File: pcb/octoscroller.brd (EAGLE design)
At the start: 71.8 x 54.6 mm, 5 parts

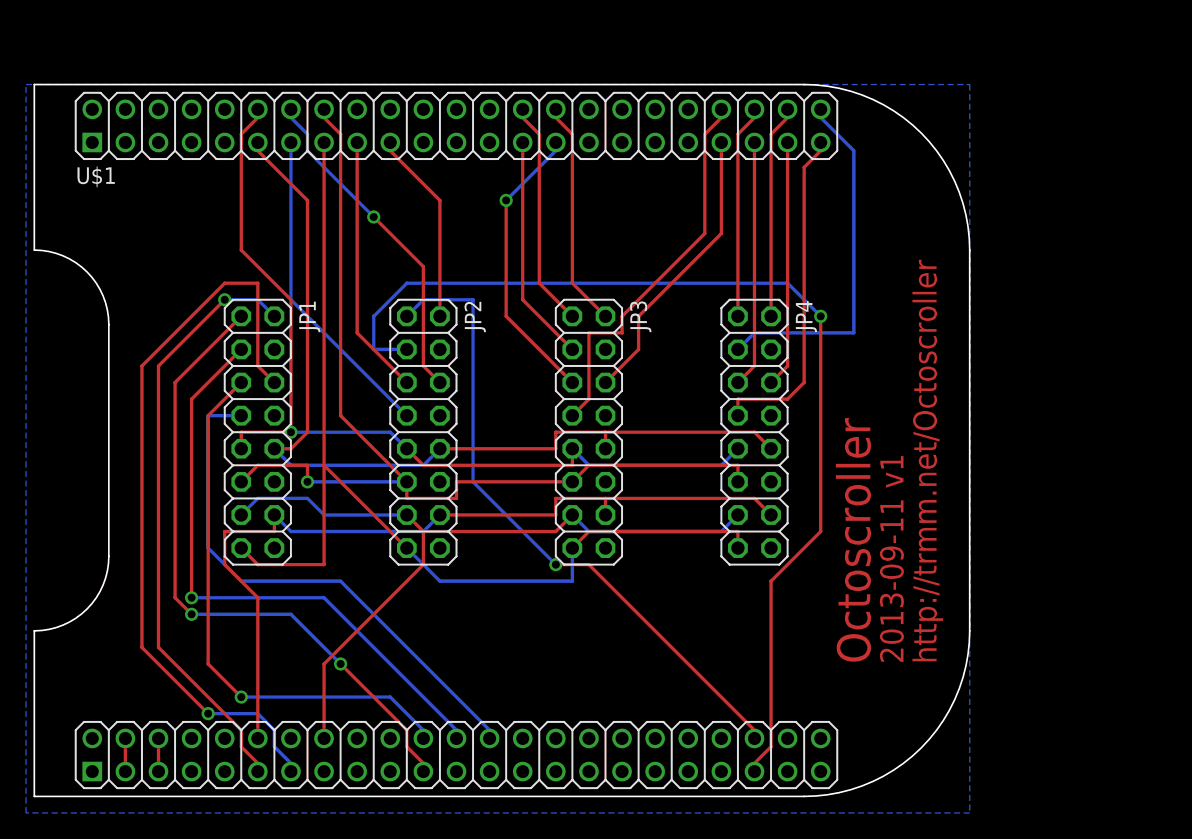
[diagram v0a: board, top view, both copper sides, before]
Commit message: octoscroller gets octo-outputs
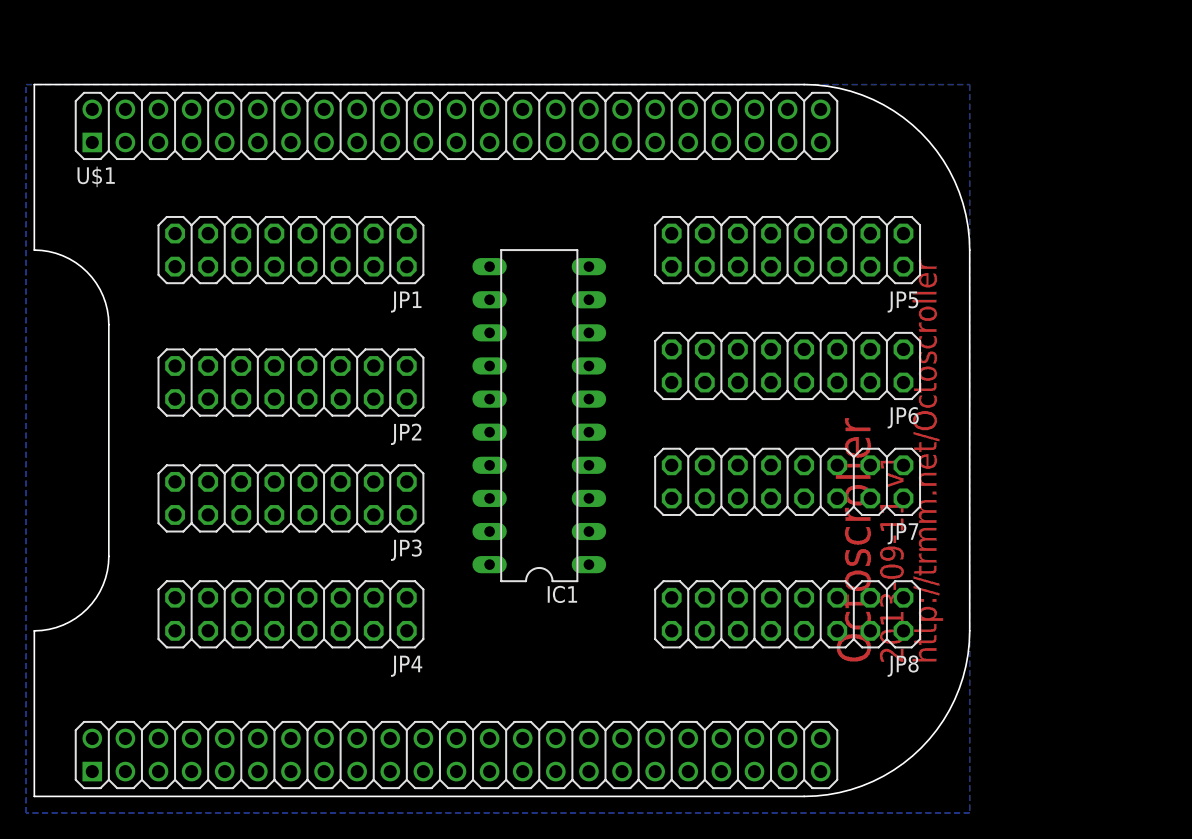
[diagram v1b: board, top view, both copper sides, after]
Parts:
- added IC1: 74LS245N, adafruit:DIL20
- added JP5, JP6, JP7, JP8: (no value), pinhead:2X08
- moved JP4 38.2 mm to (36.8, 29.2), turned to 180 degrees
- moved JP3 23.4 mm to (36.8, 38.1), turned to 180 degrees
- moved JP1 14.2 mm to (36.8, 57.1), turned to 180 degrees
- moved JP2 10.9 mm to (36.8, 47.0), turned to 180 degrees
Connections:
- new net D: JP1.12, JP2.12, JP3.12, JP4.12, JP5.12, JP6.12, JP7.12, JP8.12, U$1.15
- new net N$1: IC1.18
- new net VCC: IC1.20
- net A: now also JP5.9, JP6.9, JP7.9, JP8.9
- net B: now also JP5.10, JP6.10, JP7.10, JP8.10
- net B1: now also JP2.3, JP3.3, JP4.3, JP5.3, JP6.3, JP7.3, JP8.3
- net B2: now also JP2.7, JP3.7, JP4.7, JP5.7, JP6.7, JP7.7, JP8.7
- net B3: no longer JP2.3
- net B4: no longer JP2.7
- net B5: no longer JP3.3
- net B6: no longer JP3.7
- net B7: no longer JP4.3
- net B8: no longer JP4.7
- net C: now also JP5.11, JP6.11, JP7.11, JP8.11
- net CLK: now also JP5.13, JP6.13, JP7.13, JP8.13
- net G1: now also JP2.2, JP3.2, JP4.2, JP5.2, JP6.2, JP7.2, JP8.2
- net G2: now also JP2.6, JP3.6, JP4.6, JP5.6, JP6.6, JP7.6, JP8.6
- net G3: no longer JP2.2
- net G4: no longer JP2.6
- net G5: no longer JP3.2
- net G6: no longer JP3.6
- net G7: no longer JP4.2
- net G8: no longer JP4.6
- net GND: now also IC1.10, JP5.16, JP5.4, JP5.8, JP6.16, JP6.4, JP6.8, JP7.16, JP7.4, JP7.8, JP8.16, JP8.4, JP8.8; no longer JP1.12, JP2.12, JP3.12, JP4.12
- net LATCH: now also JP5.14, JP6.14, JP7.14, JP8.14
- net OE: now also JP5.15, JP6.15, JP7.15, JP8.15, U$1.26; no longer U$1.15
- net R1: now also JP2.1, JP3.1, JP4.1, JP5.1, JP6.1, JP7.1, JP8.1
- net R2: now also JP2.5, JP3.5, JP4.5, JP5.5, JP6.5, JP7.5, JP8.5
- net R3: no longer JP2.1
- net R4: no longer JP2.5
- net R5: no longer JP3.1
- net R6: no longer JP3.5
- net R7: no longer JP4.1
- net R8: no longer JP4.5
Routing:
- net OE: track 79.0 -> 0.00 mm
- net B3: track 78.5 -> 0.00 mm, vias 1 -> 0
- net C: track 75.4 -> 0.00 mm, vias 1 -> 0
- net A: track 69.6 -> 0.00 mm, vias 1 -> 0
- net B: track 69.1 -> 0.00 mm
- net LATCH: track 64.2 -> 0.00 mm
- net CLK: track 60.3 -> 0.00 mm
- net G2: track 57.7 -> 0.00 mm, vias 1 -> 0
- net R3: track 49.7 -> 0.00 mm, vias 1 -> 0
- net R1: track 49.4 -> 0.00 mm, vias 2 -> 0
- net G1: track 45.8 -> 0.00 mm, vias 1 -> 0
- net B1: track 45.8 -> 0.00 mm, vias 1 -> 0
- net R2: track 41.9 -> 0.00 mm, vias 1 -> 0
- net B2: track 40.7 -> 0.00 mm
- net B6: track 29.7 -> 0.00 mm
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
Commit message: octoscroller renamed outputs
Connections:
- removed net B4: U$1.13
- removed net B5: U$1.27
- removed net G3: U$1.19
- removed net G4: U$1.14
- removed net G5: U$1.30
- removed net N$1: IC1.18
- removed net R4: U$1.17
- removed net R5: U$1.28
- removed net R6: U$1.29
- new net A_RAW: IC1.18, U$1.12
- new net B1.1: JP1.3, U$1.9
- new net B1.2: JP1.7, U$1.14
- new net B2.1: JP2.3, U$1.19
- new net B2.2: JP2.7, U$1.28
- new net B3.1: JP3.3
- new net B3.2: JP3.7
- new net B4.1: JP4.3
- new net B4.2: JP4.7
- new net B5.1: JP5.3
- new net B5.2: JP5.7
- new net B6.1: JP6.3
- new net B6.2: JP6.7
- new net B7.1: JP7.3
- new net B7.2: JP7.7
- new net B8.1: JP8.3
- new net B8.2: JP8.7
- new net B_RAW: IC1.17, U$1.11
- new net CLK_RAW: IC1.13, U$1.62
- new net C_RAW: IC1.16, U$1.16
- new net D_RAW: IC1.15, U$1.15
- new net G1.1: JP1.2, U$1.8
- new net G1.2: JP1.6, U$1.10
- new net G2.1: JP2.2, U$1.18
- new net G2.2: JP2.6, U$1.29
- new net G3.1: JP3.2
- new net G3.2: JP3.6
- new net G4.1: JP4.2
- new net G4.2: JP4.6
- new net G5.1: JP5.2
- new net G5.2: JP5.6
- new net G6.1: JP6.2
- new net G6.2: JP6.6
- new net G7.1: JP7.2
- new net G7.2: JP7.6
- new net G8.1: JP8.2
- new net G8.2: JP8.6
- new net LATCH_RAW: IC1.12, U$1.58
- new net N$11: U$1.32
- new net N$12: U$1.34
- new net N$13: U$1.36
- new net N$14: U$1.38
- new net N$15: U$1.61
- new net N$16: U$1.63
- new net N$17: U$1.69
- new net N$18: U$1.71
- new net N$19: U$1.73
- new net N$20: U$1.75
- new net N$21: U$1.77
- new net N$22: U$1.60
- new net N$23: U$1.74
- new net N$24: U$1.76
- new net N$4: U$1.31
- new net N$5: U$1.33
- new net N$6: U$1.35
- new net N$7: U$1.37
- new net OE_RAW: IC1.14, U$1.26
- new net R1.1: JP1.1, U$1.7
- new net R1.2: JP1.5, U$1.13
- new net R2.1: JP2.1, U$1.17
- new net R2.2: JP2.5, U$1.27
- new net R3.1: JP3.1
- new net R3.2: JP3.5
- new net R4.1: JP4.1
- new net R4.2: JP4.5
- new net R5.1: JP5.1, U$1.30
- new net R5.2: JP5.5
- new net R6.1: JP6.1
- new net R6.2: JP6.5
- new net R7.1: JP7.1
- new net R7.2: JP7.5
- new net R8.1: JP8.1
- new net R8.2: JP8.5
- net A: now also IC1.2; no longer U$1.12
- net B: now also IC1.3; no longer U$1.11
- net B1: no longer JP1.3, JP2.3, JP3.3, JP4.3, JP5.3, JP6.3, JP7.3, JP8.3
- net B2: no longer JP1.7, JP2.7, JP3.7, JP4.7, JP5.7, JP6.7, JP7.7, JP8.7
- net C: now also IC1.4; no longer U$1.16
- net CLK: now also IC1.7; no longer U$1.62
- net D: now also IC1.5; no longer U$1.15
- net G1: no longer JP1.2, JP2.2, JP3.2, JP4.2, JP5.2, JP6.2, JP7.2, JP8.2
- net G2: no longer JP1.6, JP2.6, JP3.6, JP4.6, JP5.6, JP6.6, JP7.6, JP8.6
- net GND: now also IC1.1, IC1.19
- net LATCH: now also IC1.8; no longer U$1.58
- net OE: now also IC1.6; no longer U$1.26
- net R1: no longer JP1.1, JP2.1, JP3.1, JP4.1, JP5.1, JP6.1, JP7.1, JP8.1
- net R2: no longer JP1.5, JP2.5, JP3.5, JP4.5, JP5.5, JP6.5, JP7.5, JP8.5

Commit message: As ordered from OSH Park
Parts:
- moved IC1 25.4 mm to (30.5, 43.2), flipped to the bottom, turned to 270 degrees
- moved JP4 13.0 mm to (49.5, 26.7), turned to 0 degrees
- moved JP1 12.8 mm to (49.5, 58.4), turned to 0 degrees
- moved JP2 12.8 mm to (49.5, 48.3), turned to 0 degrees
- moved JP3 12.8 mm to (49.5, 36.8), turned to 0 degrees
- moved JP7 2.84 mm to (76.2, 36.8), turned to 0 degrees
- moved JP8 2.84 mm to (76.2, 26.7), turned to 0 degrees
- moved JP5 1.80 mm to (76.2, 58.4), turned to 0 degrees
- moved JP6 1.27 mm to (76.2, 48.3), turned to 0 degrees
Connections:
- removed net B1: U$1.70
- removed net B2: U$1.72
- removed net B3: U$1.87
- removed net B6: U$1.40
- removed net B7: U$1.46
- removed net B8: U$1.45
- removed net G1: U$1.57
- removed net G2: U$1.59
- removed net G6: U$1.39
- removed net G7: U$1.44
- removed net G8: U$1.43
- removed net N$11: U$1.32
- removed net N$12: U$1.34
- removed net N$13: U$1.36
- removed net N$14: U$1.38
- removed net N$15: U$1.61
- removed net N$16: U$1.63
- removed net N$17: U$1.69
- removed net N$18: U$1.71
- removed net N$19: U$1.73
- removed net N$20: U$1.75
- removed net N$21: U$1.77
- removed net N$22: U$1.60
- removed net N$23: U$1.74
- removed net N$24: U$1.76
- removed net N$4: U$1.31
- removed net N$5: U$1.33
- removed net N$6: U$1.35
- removed net N$7: U$1.37
- removed net R1: U$1.67
- removed net R2: U$1.68
- removed net R3: U$1.88
- removed net R7: U$1.42
- removed net R8: U$1.41
- removed net SYS_5V: U$1.53
- removed net VCC: IC1.20
- new net +5V: IC1.20, U$1.53
- net B3.1: now also U$1.59
- net B3.2: now also U$1.63
- net B4.1: now also U$1.69
- net B4.2: now also U$1.64
- net B5.1: now also U$1.31
- net B5.2: now also U$1.34
- net B6.1: now also U$1.37
- net B6.2: now also U$1.39
- net B7.1: now also U$1.43
- net B7.2: now also U$1.46
- net B8.1: now also U$1.75
- net B8.2: now also U$1.87
- net G3.1: now also U$1.60
- net G3.2: now also U$1.67
- net G4.1: now also U$1.70
- net G4.2: now also U$1.73
- net G5.1: now also U$1.32
- net G5.2: now also U$1.35
- net G6.1: now also U$1.38
- net G6.2: now also U$1.41
- net G7.1: now also U$1.44
- net G7.2: now also U$1.88
- net G8.1: now also U$1.76
- net G8.2: now also U$1.72
- net R3.1: now also U$1.57
- net R3.2: now also U$1.61
- net R4.1: now also U$1.68
- net R4.2: now also U$1.71
- net R5.2: now also U$1.33
- net R6.1: now also U$1.36
- net R6.2: now also U$1.40
- net R7.1: now also U$1.42
- net R7.2: now also U$1.45
- net R8.1: now also U$1.74
- net R8.2: now also U$1.77
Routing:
- net D: track 0.00 -> 135.9 mm, vias 0 -> 1
- net LATCH: track 0.00 -> 129.2 mm, vias 0 -> 1
- net OE: track 0.00 -> 128.2 mm, vias 0 -> 1
- net CLK: track 0.00 -> 122.3 mm, vias 0 -> 1
- net C: track 0.00 -> 121.4 mm, vias 0 -> 1
- net B: track 0.00 -> 120.7 mm, vias 0 -> 2
- net A: track 0.00 -> 114.3 mm, vias 0 -> 2
- net B7.1: track 0.00 -> 57.2 mm, vias 0 -> 1
- net OE_RAW: track 0.00 -> 45.0 mm, vias 0 -> 2
- net B7.2: track 0.00 -> 43.6 mm
- net G7.1: track 0.00 -> 43.6 mm, vias 0 -> 1
- net R7.2: track 0.00 -> 42.8 mm, vias 0 -> 1
- net +5V: track 0.00 -> 39.9 mm
- net R7.1: track 0.00 -> 37.9 mm
- net G3.2: track 0.00 -> 35.9 mm, vias 0 -> 2
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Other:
- board text added: "2013-09-30"
- board text added: "Octoscroller^2"
- board text removed: "2013-09-11 v1"
- board text removed: "Octoscroller"

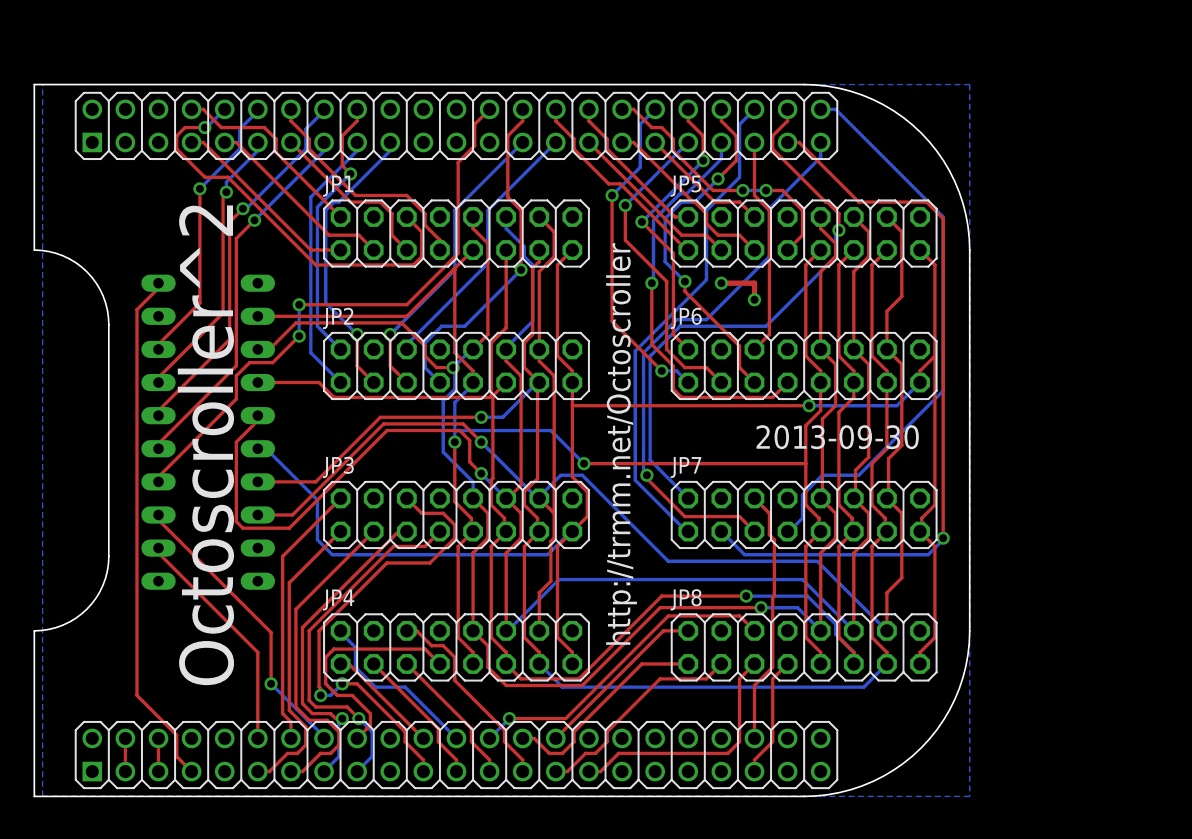
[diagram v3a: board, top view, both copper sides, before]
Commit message: reworked slightly to adjust position of connectors; ordered via oshpark
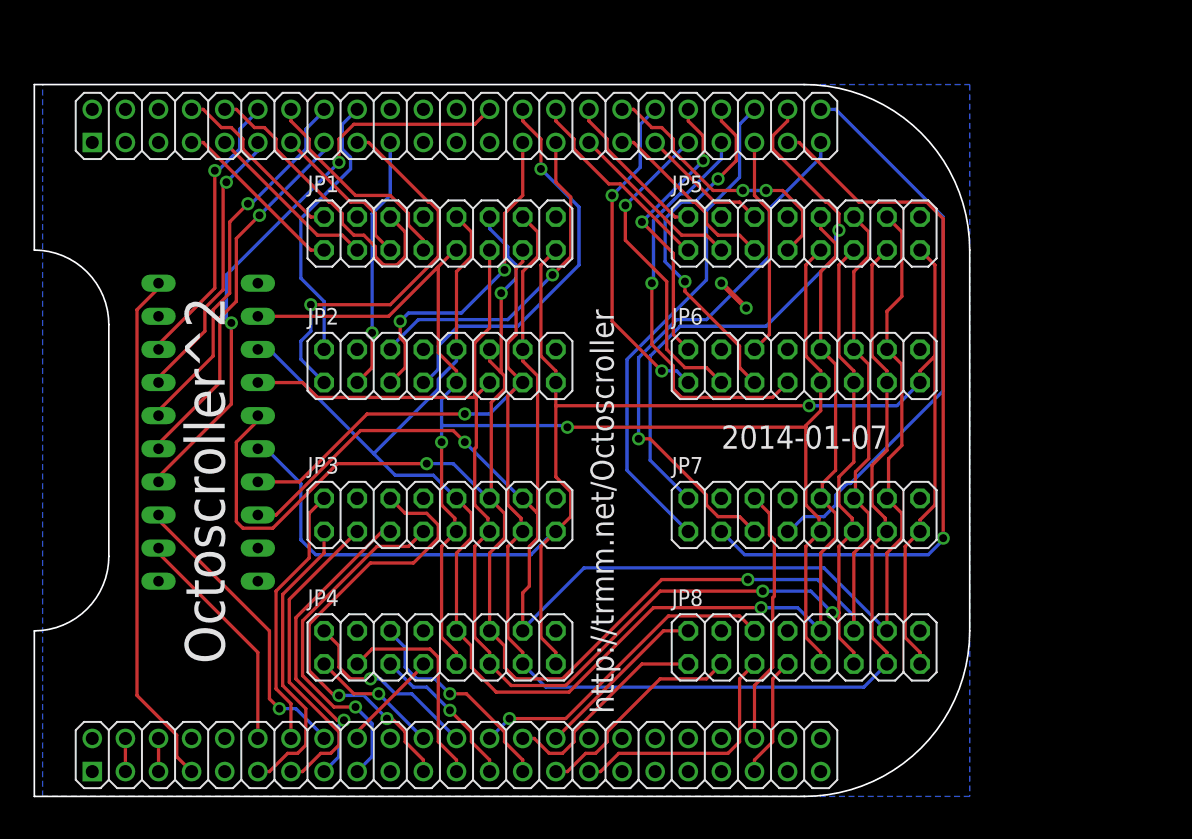
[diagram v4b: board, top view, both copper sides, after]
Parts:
- moved JP1 1.27 mm to (48.3, 58.4)
- moved JP2 1.27 mm to (48.3, 48.3)
- moved JP3 1.27 mm to (48.3, 36.8)
- moved JP4 1.27 mm to (48.3, 26.7)
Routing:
- net B4.2: track 18.2 -> 7.82 mm
- net R2.1: track 20.8 -> 30.3 mm, vias 0 -> 1
- net G1.2: track 31.8 -> 23.9 mm, vias 1 -> 0
- net G2.2: track 20.6 -> 26.1 mm, vias 0 -> 1
- net B4.1: track 10.9 -> 16.3 mm
- net B2.2: track 26.4 -> 30.4 mm
- net C: track 121.4 -> 118.4 mm, vias 1 -> 2
- net D: track 135.9 -> 138.9 mm, vias 1 -> 3
- net B2.1: track 22.2 -> 19.5 mm
- net R2.2: track 23.1 -> 25.3 mm, vias 1 -> 2
- net LATCH: track 129.2 -> 127.1 mm
- net G1.1: track 15.4 -> 14.0 mm
- net A: track 114.3 -> 113.0 mm
- net R4.1: track 8.72 -> 9.99 mm, vias 0 -> 1
- net R1.1: track 14.8 -> 13.6 mm
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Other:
- board text added: "2014-01-07"
- board text removed: "2013-09-30"

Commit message: v1.3 of boards (as ordered)
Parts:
- added +5V: 22-27-2021-02, con-molex:6410-02
- added TP1, TP2: PTR1PAD1-13, testpad:P1-13
- moved IC1 1.27 mm to (29.2, 43.2)
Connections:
- removed net VDD_5V: U$1.51, U$1.52
- new net +5V-IN: +5V.1, U$1.51, U$1.52
- net GND: now also +5V.2, TP1.TP, TP2.TP
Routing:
- net B: track 121.8 -> 136.6 mm, vias 1 -> 3
- net R3.2: track 24.2 -> 34.6 mm
- net +5V-IN: track 0.00 -> 9.53 mm
- net R2.2: track 25.3 -> 30.9 mm, vias 2 -> 1
- net G2.2: track 26.1 -> 21.7 mm, vias 1 -> 0
- net B2.2: track 30.4 -> 26.1 mm
- net A: track 113.0 -> 117.1 mm, vias 2 -> 3
- net G3.2: track 34.7 -> 31.5 mm
- net VDD_5V: track 2.54 -> 0.00 mm
- net OE_RAW: track 44.8 -> 47.0 mm
- net D: track 138.9 -> 140.7 mm
- net R2.1: track 30.3 -> 32.0 mm
- net OE: track 128.9 -> 127.2 mm, vias 1 -> 4
- net LATCH_RAW: track 17.8 -> 19.3 mm
- net C: track 118.4 -> 119.6 mm
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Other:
- board text added: "2014-05-05"
- board text added: "GND"
- board text added: "Octoscroller^2 v1.3"
- board text removed: "2014-01-07"
- board text removed: "Octoscroller^2"
